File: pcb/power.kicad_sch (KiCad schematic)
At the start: 60 parts, among them J7 1S LiPo, Q1 Q_Dual_NMOS_S1G1S2G2D2D2D1D1, Q2 Q_Dual_NMOS_S1G1S2G2D2D2D1D1, Q3 Q_Dual_NMOS_S1G1S2G2D2D2D1D1, U13 BQ25798, U14 TPS63060, U15 TPS61089

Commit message: select the inductors, and take two footprints from the processor's reference design
Four parts, and two of them are the same one. The core regulator takes the part its own vendor
names. The charger takes a Coilcraft XGL4030-102MEC, and the 3.3V converter takes the same part
again: it needs only 3A where the charger needs 7, but one part number, one land pattern and one
thing to stock is worth more than the margin it wastes, and it has lower resistance than the part
that converter's vendor suggests. The 5V boost keeps the Wurth part from its vendor's own list.

Saturation quoted against an inductance droop rather than as a single number is what made these
comparable. The charger needs about 7A at worst. The first part considered reaches that only at a
30% droop, which would feed back into more ripple and a higher peak again; the one chosen is still
holding 80% of its inductance there, for a millimetre of extra height in the same 4mm footprint and
lower resistance as well.

Two footprints now come from the processor vendor's published reference design, which is MIT
licensed and carried in with the notice that licence requires. One is the core inductor's, which no
stock library had. The other is the processor's own land pattern, and that settles one of the four
packages fitted provisionally: the pad under it is no longer the nearest library variant but the
pattern its maker lays out. Three provisional packages remain, and so does the land pattern for the
two Coilcraft parts, which is a single drawing covering both.

133 of 135 parts now carry a footprint.

Co-Authored-By: Claude Opus 5 (1M context) <noreply@anthropic.com>
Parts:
- L10: Isat 7A -> 7.6A @20%; MPN (none) -> Coilcraft XGL4030-102MEC
- L11: Isat 3A -> 7.6A @20%; MPN (none) -> Coilcraft XGL4030-102MEC
- L12: Isat 7A -> 13A; MPN (none) -> Wurth 744311220
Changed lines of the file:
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@@
+			)
+		)
+		(property "MPN" "Coilcraft XGL4030-102MEC"
+			(at 207.01 121.92 0)
+			(show_name no)
+			(do_not_autoplace no)
+			(effects
+				(font
+					(size 1.27 1.27)
+				)
+				(hide yes)
 			)
 		)
@@
 			)
 		)
-		(property "Isat" "7A"
+		(property "Isat" "7.6A @20%"
 			(at 207.01 121.92 0)
 			(show_name no)
@@
 			)
 		)
+		(property "MPN" "Coilcraft XGL4030-102MEC"
+			(at 241.3 114.3 0)
+			(show_name no)
+			(do_not_autoplace no)
+			(effects
+				(font
+					(size 1.27 1.27)
+				)
+				(hide yes)
+			)
+		)
 		(property "Tolerance" "20%"
 			(at 241.3 114.3 0)
@@
 			)
 		)
-		(property "Isat" "3A"
+		(property "Isat" "7.6A @20%"
 			(at 241.3 114.3 0)
 			(show_name no)
@@
 			)
 		)
+		(property "MPN" "Wurth 744311220"
+			(at 243.586 160.528 0)
+			(show_name no)
+			(do_not_autoplace no)
+			(effects
+				(font
+					(size 1.27 1.27)
+				)
+				(hide yes)
+			)
+		)
 		(property "Tolerance" "20%"
 			(at 243.586 160.528 0)
@@
 			)
 		)
-		(property "Isat" "7A"
+		(property "Isat" "13A"
 			(at 243.586 160.528 0)
 			(show_name no)

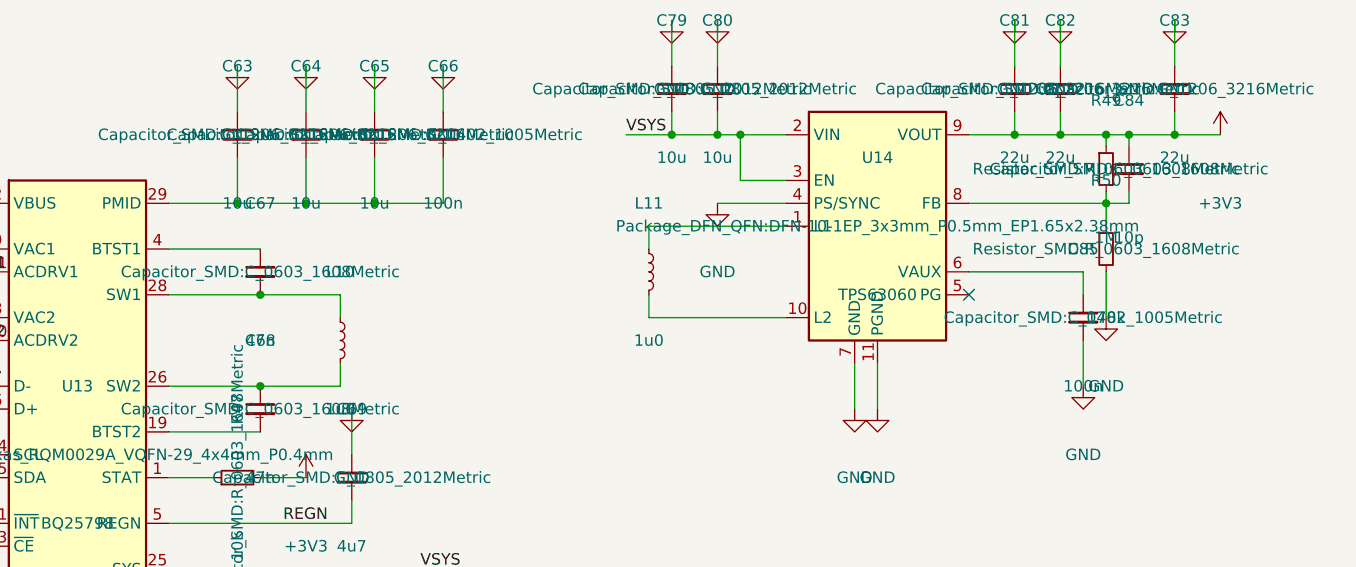
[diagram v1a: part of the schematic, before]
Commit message: finish the footprints, and check the provisional ones against their vendors
Every one of the 135 parts now carries a footprint. The three that were fitted by matching body size
and pin count have been checked against their makers' own data, and two of the three were wrong.

The 3.3V converter's was wrong in kind rather than by a margin. Its maker's land pattern puts a
shaped thermal pad under the part -- a centre rectangle with fingers and tabs, thirteen pieces in
all -- and gives the signal pads extended toes beyond the body. The generic entry has a plain
rectangle and no toes. That shape is the thing in the drawing I could not interpret earlier and
assumed was a drafting flourish; it is the pattern. The library carries the real one under the
vendor's package code.

The hub's was wrong by 0.2mm each way. Its datasheet tabulates a recommended land pattern, not just
a package outline, and names a 3.70mm pad where the provisional entry had 3.90. Too large is the
direction that floats a part off its pins.

The power sink's was right: its vendor's exposed pad is 1.70 x 2.40 nominal against the fitted
1.65 x 2.38, a few hundredths under, which is the safe side. Worth confirming rather than assuming.

The two inductors took a footprint the library keeps under a family name, and its 4mm entries at
both heights carry identical pads -- which independently confirms the shared land pattern that made
the taller, higher-current part a free swap when it was chosen.

The hit rate is the lesson. Picking a footprint by body size and pin count got two of three wrong,
and neither error would have shown in the schematic, the netlist or any rules check -- only on a
board that did not assemble properly.

Co-Authored-By: Claude Opus 5 (1M context) <noreply@anthropic.com>
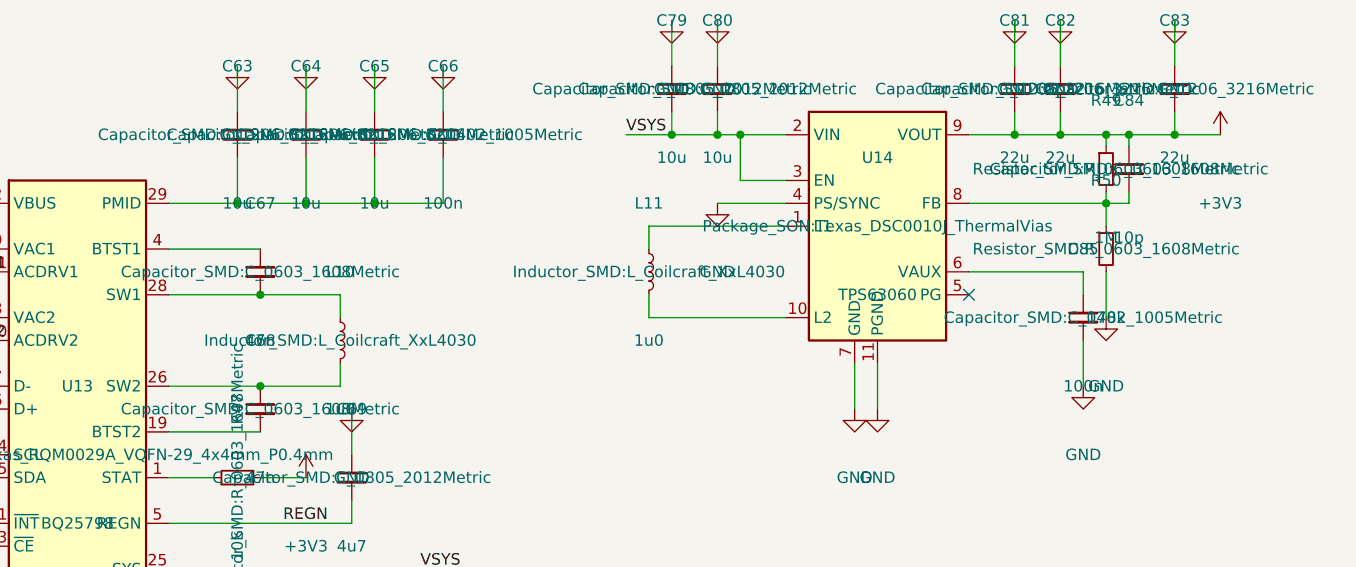
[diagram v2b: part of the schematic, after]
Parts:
- L10, L11: footprint (none) -> Inductor_SMD:L_Coilcraft_XxL4030
- U14: footprint Package_DFN_QFN:DFN-10-1EP_3x3mm_P0.5mm_EP1.65x2.38mm -> Package_SON:Texas_DSC0010J_ThermalVias
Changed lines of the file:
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@@
 			)
 		)
-		(property "Footprint" ""
+		(property "Footprint" "Inductor_SMD:L_Coilcraft_XxL4030"
 			(at 207.01 114.3 0)
 			(show_name no)
@@
 			)
 		)
-		(property "Footprint" ""
+		(property "Footprint" "Inductor_SMD:L_Coilcraft_XxL4030"
 			(at 241.3 106.68 0)
 			(show_name no)
@@
 			)
 		)
-		(property "Footprint" "Package_DFN_QFN:DFN-10-1EP_3x3mm_P0.5mm_EP1.65x2.38mm"
+		(property "Footprint" "Package_SON:Texas_DSC0010J_ThermalVias"
 			(at 266.7 101.6 0)
 			(show_name no)
